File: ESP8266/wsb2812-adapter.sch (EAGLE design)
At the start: 4 parts, among them CON1 USBMICRO-NO_CENTER

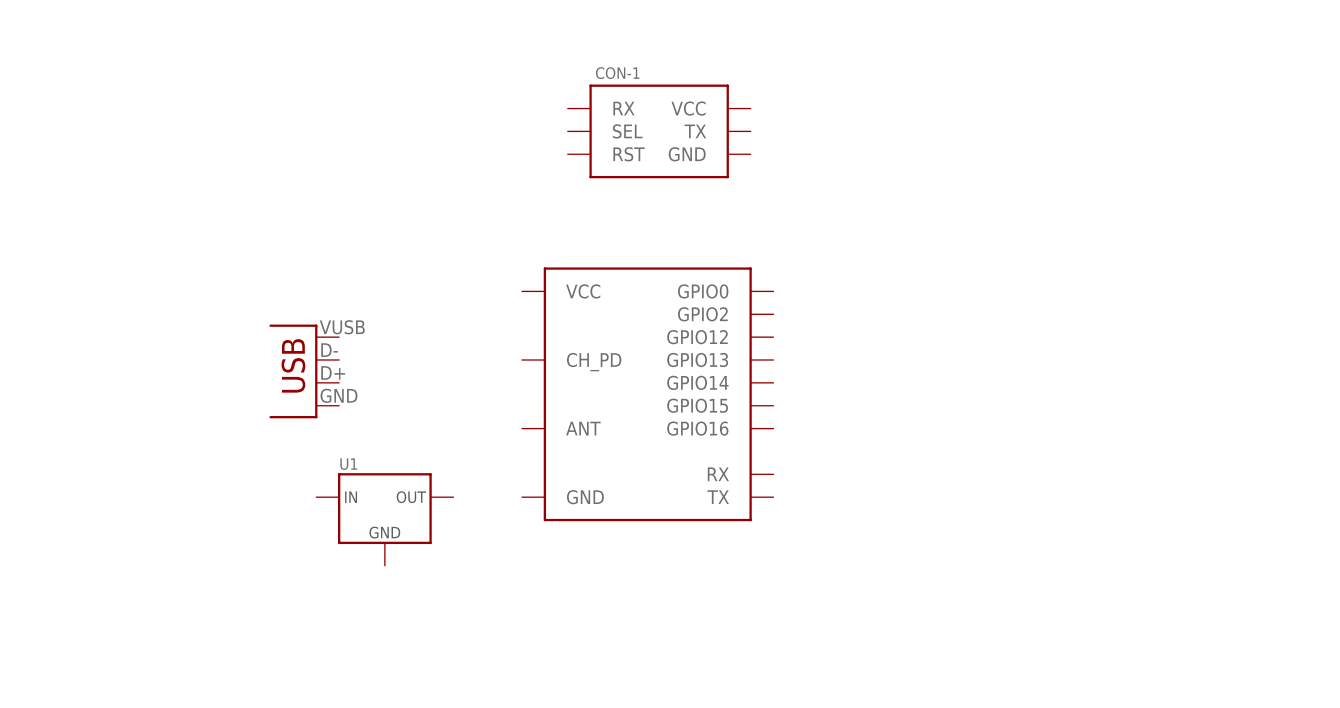
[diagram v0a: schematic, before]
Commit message: added power supply
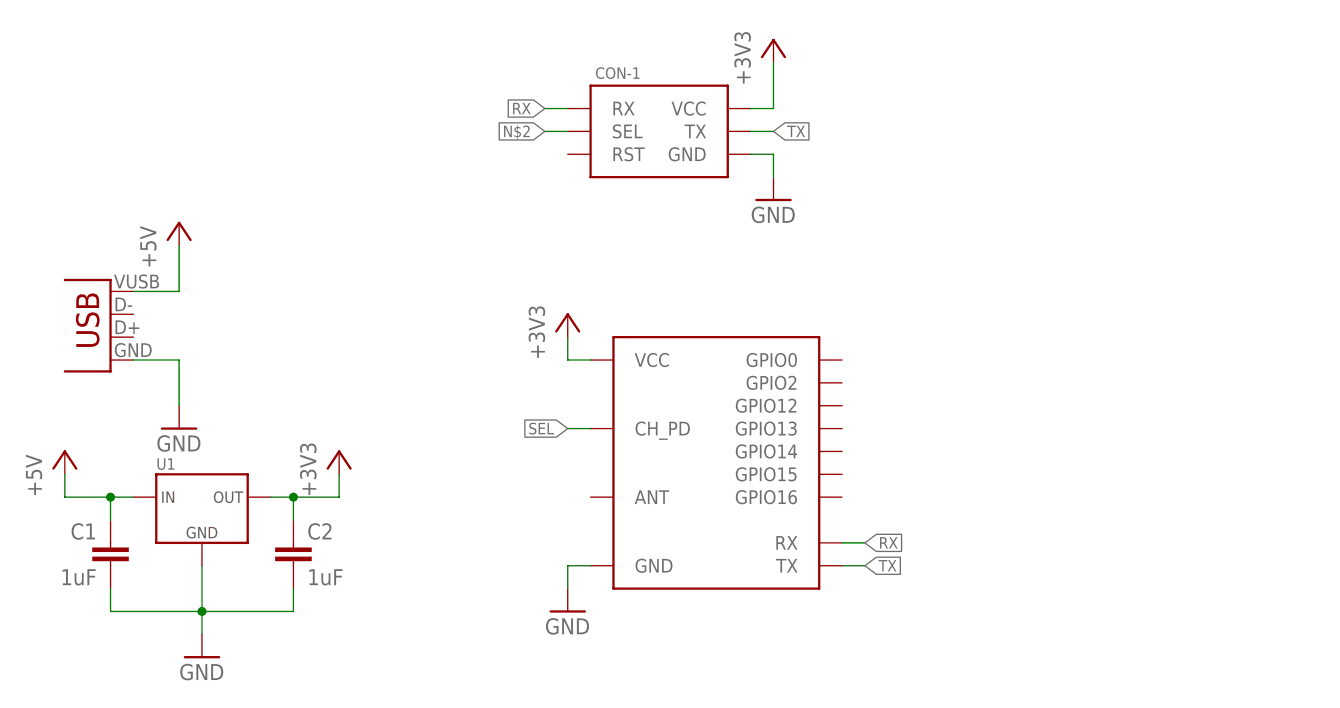
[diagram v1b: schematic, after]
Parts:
- added C1, C2: 1uF, p.peter-rcl:C-EUC0805
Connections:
- new net +3V3: C2.1, CON-1.VCC, U$1.VCC, U1.OUT
- new net +5V: C1.1, CON1.VBUS, U1.IN
- new net GND: C1.2, C2.2, CON-1.GND, CON1.GND, U$1.GND, U1.GND
- new net N$2: CON-1.SEL
- new net RX: CON-1.RX, U$1.RX
- new net SEL: U$1.CH_PD
- new net TX: CON-1.TX, U$1.TX
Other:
- moved on the sheet: U1
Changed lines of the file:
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@@
 <?xml version="1.0" encoding="utf-8"?>
 <!DOCTYPE eagle SYSTEM "eagle.dtd">
-<eagle version="7.3.0">
+<eagle version="7.1.0">
 <drawing>
 <settings>
@@
 <part name="CON-1" library="p.peter-connectors" deviceset="ESP8266-6_PIN" device="-POGO"/>
 <part name="U1" library="p.peter-regulators" deviceset="REGULATOR-XC6206" device="SOT23"/>
+<part name="P+1" library="supply1" deviceset="+5V" device=""/>
+<part name="+3V1" library="supply1" deviceset="+3V3" device=""/>
+<part name="GND1" library="supply1" deviceset="GND" device=""/>
+<part name="C1" library="p.peter-rcl" deviceset="C-EU" device="C0805" value="1uF"/>
+<part name="C2" library="p.peter-rcl" deviceset="C-EU" device="C0805" value="1uF"/>
+<part name="GND2" library="supply1" deviceset="GND" device=""/>
+<part name="P+2" library="supply1" deviceset="+5V" device=""/>
+<part name="GND3" library="supply1" deviceset="GND" device=""/>
+<part name="+3V2" library="supply1" deviceset="+3V3" device=""/>
+<part name="+3V3" library="supply1" deviceset="+3V3" device=""/>
+<part name="GND4" library="supply1" deviceset="GND" device=""/>
 </parts>
 <sheets>
@@
 </plain>
 <instances>
-<instance part="U$1" gate="G$1" x="35.56" y="50.8"/>
-<instance part="CON1" gate="G$1" x="-2.54" y="50.8"/>
+<instance part="U$1" gate="G$1" x="43.18" y="43.18"/>
+<instance part="CON1" gate="G$1" x="-25.4" y="55.88"/>
 <instance part="CON-1" gate="G$1" x="35.56" y="78.74"/>
-<instance part="U1" gate="G$1" x="5.08" y="38.1"/>
+<instance part="U1" gate="G$1" x="-15.24" y="38.1"/>
+<instance part="P+1" gate="1" x="-30.48" y="43.18"/>
+<instance part="+3V1" gate="G$1" x="0" y="43.18"/>
+<instance part="GND1" gate="1" x="-15.24" y="20.32"/>
+<instance part="C1" gate="G$1" x="-25.4" y="33.02" rot="MR0"/>
+<instance part="C2" gate="G$1" x="-5.08" y="33.02"/>
+<instance part="GND2" gate="1" x="-17.78" y="45.72"/>
+<instance part="P+2" gate="1" x="-17.78" y="68.58"/>
+<instance part="GND3" gate="1" x="25.4" y="25.4"/>
+<instance part="+3V2" gate="G$1" x="25.4" y="58.42"/>
+<instance part="+3V3" gate="G$1" x="48.26" y="88.9"/>
+<instance part="GND4" gate="1" x="48.26" y="71.12"/>
 </instances>
 <busses>
 </busses>
 <nets>
+<net name="+5V" class="0">
+<segment>
+<pinref part="P+1" gate="1" pin="+5V"/>
+<pinref part="U1" gate="G$1" pin="IN"/>
+<wire x1="-22.86" y1="38.1" x2="-25.4" y2="38.1" width="0.1524" layer="91"/>
+<wire x1="-25.4" y1="38.1" x2="-30.48" y2="38.1" width="0.1524" layer="91"/>
+<wire x1="-30.48" y1="38.1" x2="-30.48" y2="40.64" width="0.1524" layer="91"/>
+<pinref part="C1" gate="G$1" pin="1"/>
+<wire x1="-25.4" y1="35.56" x2="-25.4" y2="38.1" width="0.1524" layer="91"/>
+<junction x="-25.4" y="38.1"/>
+</segment>
+<segment>
+<pinref part="CON1" gate="G$1" pin="VBUS"/>
+<wire x1="-22.86" y1="60.96" x2="-17.78" y2="60.96" width="0.1524" layer="91"/>
+<wire x1="-17.78" y1="60.96" x2="-17.78" y2="66.04" width="0.1524" layer="91"/>
+<pinref part="P+2" gate="1" pin="+5V"/>
+</segment>
+</net>
+<net name="+3V3" class="0">
+<segment>
+<pinref part="U1" gate="G$1" pin="OUT"/>
+<pinref part="+3V1" gate="G$1" pin="+3V3"/>
+<wire x1="0" y1="40.64" x2="0" y2="38.1" width="0.1524" layer="91"/>
+<wire x1="0" y1="38.1" x2="-5.08" y2="38.1" width="0.1524" layer="91"/>
+<wire x1="-5.08" y1="38.1" x2="-7.62" y2="38.1" width="0.1524" layer="91"/>
+<pinref part="C2" gate="G$1" pin="1"/>
+<wire x1="-5.08" y1="35.56" x2="-5.08" y2="38.1" width="0.1524" layer="91"/>
+<junction x="-5.08" y="38.1"/>
+</segment>
+<segment>
+<pinref part="U$1" gate="G$1" pin="VCC"/>
+<wire x1="27.94" y1="53.34" x2="25.4" y2="53.34" width="0.1524" layer="91"/>
+<wire x1="25.4" y1="53.34" x2="25.4" y2="55.88" width="0.1524" layer="91"/>
+<pinref part="+3V2" gate="G$1" pin="+3V3"/>
+</segment>
+<segment>
+<pinref part="CON-1" gate="G$1" pin="VCC"/>
+<wire x1="45.72" y1="81.28" x2="48.26" y2="81.28" width="0.1524" layer="91"/>
+<wire x1="48.26" y1="81.28" x2="48.26" y2="86.36" width="0.1524" layer="91"/>
+<pinref part="+3V3" gate="G$1" pin="+3V3"/>
+</segment>
+</net>
+<net name="GND" class="0">
+<segment>
+<pinref part="U1" gate="G$1" pin="GND"/>
+<pinref part="GND1" gate="1" pin="GND"/>
+<wire x1="-15.24" y1="22.86" x2="-15.24" y2="25.4" width="0.1524" layer="91"/>
+<pinref part="C1" gate="G$1" pin="2"/>
+<wire x1="-15.24" y1="25.4" x2="-15.24" y2="30.48" width="0.1524" layer="91"/>
+<wire x1="-25.4" y1="27.94" x2="-25.4" y2="25.4" width="0.1524" layer="91"/>
+<wire x1="-25.4" y1="25.4" x2="-22.86" y2="25.4" width="0.1524" layer="91"/>
+<wire x1="-22.86" y1="25.4" x2="-15.24" y2="25.4" width="0.1524" layer="91"/>
+<wire x1="-15.24" y1="25.4" x2="-7.62" y2="25.4" width="0.1524" layer="91"/>
+<pinref part="C2" gate="G$1" pin="2"/>
+<wire x1="-7.62" y1="25.4" x2="-5.08" y2="25.4" width="0.1524" layer="91"/>
+<wire x1="-5.08" y1="25.4" x2="-5.08" y2="27.94" width="0.1524" layer="91"/>
+<junction x="-15.24" y="25.4"/>
+</segment>
+<segment>
+<pinref part="CON1" gate="G$1" pin="GND"/>
+<wire x1="-22.86" y1="53.34" x2="-17.78" y2="53.34" width="0.1524" layer="91"/>
+<wire x1="-17.78" y1="53.34" x2="-17.78" y2="48.26" width="0.1524" layer="91"/>
+<pinref part="GND2" gate="1" pin="GND"/>
+</segment>
+<segment>
+<pinref part="U$1" gate="G$1" pin="GND"/>
+<wire x1="27.94" y1="30.48" x2="25.4" y2="30.48" width="0.1524" layer="91"/>
+<wire x1="25.4" y1="30.48" x2="25.4" y2="27.94" width="0.1524" layer="91"/>
+<pinref part="GND3" gate="1" pin="GND"/>
+</segment>
+<segment>
+<pinref part="CON-1" gate="G$1" pin="GND"/>
+<wire x1="45.72" y1="76.2" x2="48.26" y2="76.2" width="0.1524" layer="91"/>
+<wire x1="48.26" y1="76.2" x2="48.26" y2="73.66" width="0.1524" layer="91"/>
+<pinref part="GND4" gate="1" pin="GND"/>
+</segment>
+</net>
+<net name="SEL" class="0">
+<segment>
+<pinref part="U$1" gate="G$1" pin="CH_PD"/>
+<wire x1="27.94" y1="45.72" x2="25.4" y2="45.72" width="0.1524" layer="91"/>
+<label x="25.4" y="45.72" size="1.27" layer="95" rot="R180" xref="yes"/>
+</segment>
+</net>
+<net name="RX" class="0">
+<segment>
+<pinref part="U$1" gate="G$1" pin="RX"/>
+<wire x1="55.88" y1="33.02" x2="58.42" y2="33.02" width="0.1524" layer="91"/>
+<label x="58.42" y="33.02" size="1.27" layer="95" xref="yes"/>
+</segment>
+<segment>
+<pinref part="CON-1" gate="G$1" pin="RX"/>
+<wire x1="25.4" y1="81.28" x2="22.86" y2="81.28" width="0.1524" layer="91"/>
+<label x="22.86" y="81.28" size="1.27" layer="95" rot="R180" xref="yes"/>
+</segment>
+</net>
+<net name="TX" class="0">
+<segment>
+<pinref part="U$1" gate="G$1" pin="TX"/>
+<wire x1="55.88" y1="30.48" x2="58.42" y2="30.48" width="0.1524" layer="91"/>
+<label x="58.42" y="30.48" size="1.27" layer="95" xref="yes"/>
+</segment>
+<segment>
+<pinref part="CON-1" gate="G$1" pin="TX"/>
+<wire x1="45.72" y1="78.74" x2="48.26" y2="78.74" width="0.1524" layer="91"/>
+<label x="48.26" y="78.74" size="1.27" layer="95" xref="yes"/>
+</segment>
+</net>
+<net name="N$2" class="0">
+<segment>
+<pinref part="CON-1" gate="G$1" pin="SEL"/>
+<wire x1="25.4" y1="78.74" x2="22.86" y2="78.74" width="0.1524" layer="91"/>
+<label x="22.86" y="78.74" size="1.27" layer="95" rot="R180" xref="yes"/>
+</segment>
+</net>
 </nets>
 </sheet>

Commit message: V0.1 done
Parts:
- added +5V, GND: PTR1PAD1-20, testpad:PTR1PAD1-20
- added DAT: (no value), pinhead:PINHD-1X1
- added R1, R2, R3: 10k, p.peter-rcl:R-EU_R0603
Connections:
- removed net SEL: U$1.CH_PD
- new net FLASH: CON-1.SEL, U$1.GPIO0
- new net N$1: R1.1, U$1.GPIO15
- new net N$3: R2.1, U$1.GPIO2
- new net RESET: CON-1.RST, R3.1, U$1.CH_PD
- net +3V3: now also R2.2, R3.2
- net +5V: now also +5V.TP
- net GND: now also GND.TP, R1.2
- net N$2: now also DAT.1, U$1.GPIO12; no longer CON-1.SEL
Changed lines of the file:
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@@
 <?xml version="1.0" encoding="utf-8"?>
 <!DOCTYPE eagle SYSTEM "eagle.dtd">
-<eagle version="7.1.0">
+<eagle version="7.3.0">
 <drawing>
 <settings>
@@
 <part name="+3V3" library="supply1" deviceset="+3V3" device=""/>
 <part name="GND4" library="supply1" deviceset="GND" device=""/>
+<part name="R1" library="p.peter-rcl" deviceset="R-EU_" device="R0603" value="10k"/>
+<part name="GND5" library="supply1" deviceset="GND" device=""/>
+<part name="R2" library="p.peter-rcl" deviceset="R-EU_" device="R0603" value="10k"/>
+<part name="+3V4" library="supply1" deviceset="+3V3" device=""/>
+<part name="R3" library="p.peter-rcl" deviceset="R-EU_" device="R0603" value="10k"/>
+<part name="+3V5" library="supply1" deviceset="+3V3" device=""/>
+<part name="+5V" library="testpad" deviceset="PTR1" device="PAD1-20"/>
+<part name="GND" library="testpad" deviceset="PTR1" device="PAD1-20"/>
+<part name="DAT" library="pinhead" deviceset="PINHD-1X1" device=""/>
+<part name="P+3" library="supply1" deviceset="+5V" device=""/>
+<part name="GND6" library="supply1" deviceset="GND" device=""/>
 </parts>
 <sheets>
@@
 <instance part="P+2" gate="1" x="-17.78" y="68.58"/>
 <instance part="GND3" gate="1" x="25.4" y="25.4"/>
-<instance part="+3V2" gate="G$1" x="25.4" y="58.42"/>
+<instance part="+3V2" gate="G$1" x="25.4" y="63.5"/>
 <instance part="+3V3" gate="G$1" x="48.26" y="88.9"/>
 <instance part="GND4" gate="1" x="48.26" y="71.12"/>
+<instance part="R1" gate="G$1" x="63.5" y="40.64"/>
+<instance part="GND5" gate="1" x="73.66" y="25.4"/>
+<instance part="R2" gate="G$1" x="71.12" y="50.8"/>
+<instance part="+3V4" gate="G$1" x="78.74" y="63.5"/>
+<instance part="R3" gate="G$1" x="17.78" y="53.34" rot="R90"/>
+<instance part="+3V5" gate="G$1" x="17.78" y="63.5"/>
+<instance part="+5V" gate="G$1" x="101.6" y="50.8"/>
+<instance part="GND" gate="G$1" x="106.68" y="50.8"/>
+<instance part="DAT" gate="G$1" x="88.9" y="45.72"/>
+<instance part="P+3" gate="1" x="101.6" y="58.42"/>
+<instance part="GND6" gate="1" x="106.68" y="58.42" rot="R180"/>
 </instances>
 <busses>
@@
 <pinref part="P+2" gate="1" pin="+5V"/>
 </segment>
+<segment>
+<pinref part="+5V" gate="G$1" pin="TP"/>
+<pinref part="P+3" gate="1" pin="+5V"/>
+<wire x1="101.6" y1="55.88" x2="101.6" y2="53.34" width="0.1524" layer="91"/>
+</segment>
 </net>
 <net name="+3V3" class="0">
@@
 <pinref part="U$1" gate="G$1" pin="VCC"/>
 <wire x1="27.94" y1="53.34" x2="25.4" y2="53.34" width="0.1524" layer="91"/>
-<wire x1="25.4" y1="53.34" x2="25.4" y2="55.88" width="0.1524" layer="91"/>
+<wire x1="25.4" y1="53.34" x2="25.4" y2="60.96" width="0.1524" layer="91"/>
 <pinref part="+3V2" gate="G$1" pin="+3V3"/>
 </segment>
@@
 <wire x1="48.26" y1="81.28" x2="48.26" y2="86.36" width="0.1524" layer="91"/>
 <pinref part="+3V3" gate="G$1" pin="+3V3"/>
+</segment>
+<segment>
+<pinref part="R2" gate="G$1" pin="2"/>
+<wire x1="76.2" y1="50.8" x2="78.74" y2="50.8" width="0.1524" layer="91"/>
+<wire x1="78.74" y1="50.8" x2="78.74" y2="60.96" width="0.1524" layer="91"/>
+<pinref part="+3V4" gate="G$1" pin="+3V3"/>
+</segment>
+<segment>
+<pinref part="R3" gate="G$1" pin="2"/>
+<pinref part="+3V5" gate="G$1" pin="+3V3"/>
+<wire x1="17.78" y1="60.96" x2="17.78" y2="58.42" width="0.1524" layer="91"/>
 </segment>
 </net>
@@
 <pinref part="GND4" gate="1" pin="GND"/>
 </segment>
-</net>
-<net name="SEL" class="0">
-<segment>
-<pinref part="U$1" gate="G$1" pin="CH_PD"/>
-<wire x1="27.94" y1="45.72" x2="25.4" y2="45.72" width="0.1524" layer="91"/>
-<label x="25.4" y="45.72" size="1.27" layer="95" rot="R180" xref="yes"/>
+<segment>
+<pinref part="R1" gate="G$1" pin="2"/>
+<wire x1="68.58" y1="40.64" x2="71.12" y2="40.64" width="0.1524" layer="91"/>
+<wire x1="71.12" y1="40.64" x2="73.66" y2="40.64" width="0.1524" layer="91"/>
+<wire x1="73.66" y1="40.64" x2="73.66" y2="27.94" width="0.1524" layer="91"/>
+<pinref part="GND5" gate="1" pin="GND"/>
+</segment>
+<segment>
+<pinref part="GND" gate="G$1" pin="TP"/>
+<pinref part="GND6" gate="1" pin="GND"/>
+<wire x1="106.68" y1="55.88" x2="106.68" y2="53.34" width="0.1524" layer="91"/>
 </segment>
 </net>
@@
 </segment>
 </net>
-<net name="N$2" class="0">
+<net name="FLASH" class="0">
+<segment>
+<pinref part="U$1" gate="G$1" pin="GPIO0"/>
+<wire x1="55.88" y1="53.34" x2="58.42" y2="53.34" width="0.1524" layer="91"/>
+<label x="58.42" y="53.34" size="1.27" layer="95" ratio="12" xref="yes"/>
+</segment>
 <segment>
 <pinref part="CON-1" gate="G$1" pin="SEL"/>
@@
 </segment>
 </net>
+<net name="RESET" class="0">
+<segment>
+<pinref part="CON-1" gate="G$1" pin="RST"/>
+<wire x1="25.4" y1="76.2" x2="22.86" y2="76.2" width="0.1524" layer="91"/>
+<label x="22.86" y="76.2" size="1.27" layer="95" ratio="12" rot="R180" xref="yes"/>
+</segment>
+<segment>
+<pinref part="U$1" gate="G$1" pin="CH_PD"/>
+<wire x1="27.94" y1="45.72" x2="17.78" y2="45.72" width="0.1524" layer="91"/>
+<label x="12.7" y="45.72" size="1.27" layer="95" rot="R180" xref="yes"/>
+<pinref part="R3" gate="G$1" pin="1"/>
+<wire x1="17.78" y1="45.72" x2="12.7" y2="45.72" width="0.1524" layer="91"/>
+<wire x1="17.78" y1="48.26" x2="17.78" y2="45.72" width="0.1524" layer="91"/>
+<junction x="17.78" y="45.72"/>
+</segment>
+</net>
+<net name="N$1" class="0">
+<segment>
+<pinref part="U$1" gate="G$1" pin="GPIO15"/>
+<pinref part="R1" gate="G$1" pin="1"/>
+<wire x1="55.88" y1="40.64" x2="58.42" y2="40.64" width="0.1524" layer="91"/>
+</segment>
+</net>
+<net name="N$3" class="0">
+<segment>
+<pinref part="U$1" gate="G$1" pin="GPIO2"/>
+<pinref part="R2" gate="G$1" pin="1"/>
+<wire x1="66.04" y1="50.8" x2="55.88" y2="50.8" width="0.1524" layer="91"/>
+</segment>
+</net>
+<net name="N$2" class="0">
+<segment>
+<pinref part="U$1" gate="G$1" pin="GPIO12"/>
+<wire x1="55.88" y1="48.26" x2="63.5" y2="48.26" width="0.1524" layer="91"/>
+<wire x1="63.5" y1="48.26" x2="63.5" y2="45.72" width="0.1524" layer="91"/>
+<pinref part="DAT" gate="G$1" pin="1"/>
+<wire x1="63.5" y1="45.72" x2="86.36" y2="45.72" width="0.1524" layer="91"/>
+</segment>
+</net>
